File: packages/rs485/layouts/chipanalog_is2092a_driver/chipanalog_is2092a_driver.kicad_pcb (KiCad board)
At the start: 2 copper layers, 7 parts

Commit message: Rebuild all
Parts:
- turned U1 to 0 degrees
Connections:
- net hv-1 renamed VDDP
- net line renamed A
- net line-1 renamed DI
- net line-3 renamed RO
- net line-4 renamed B
- net transceiver-line renamed SEL
- C1 pad 1: hv -> VDDL
- C2 pad 1: hv-2 -> hv
- C4 pad 1: hv-2 -> hv
- C6 pad 1: hv-2 -> hv
- U1 pad 10: hv-2 -> hv
- U1 pad 11: hv-2 -> hv
- U1 pad 2: line-2 -> REh
- U1 pad 3: line-2 -> DE
- U1 pad 7: hv -> VDDL
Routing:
- net (no net): track 0.00 -> 13.7 mm
- net hv-2: track 5.88 -> 0.00 mm
- net VDDP: track 3.56 -> 0.00 mm
- net line-2: track 2.62 -> 0.00 mm
- net hv: track 1.65 -> 0.00 mm

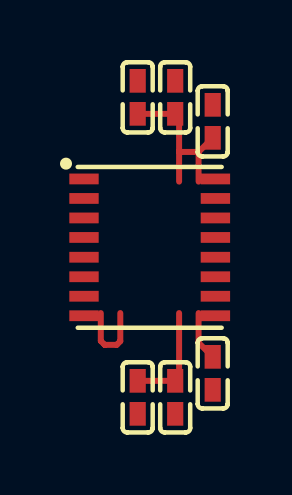
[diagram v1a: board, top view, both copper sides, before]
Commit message: Fix LDO power in voltage range
Fix RS485 sp3485 and is2092 RE WE connections
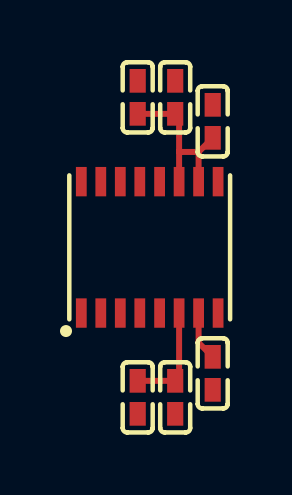
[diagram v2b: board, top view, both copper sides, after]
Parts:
- turned U1 to 90 degrees
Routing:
- net (no net): track 13.7 -> 0.00 mm
- net hv: track 0.00 -> 5.88 mm
- net VDDP: track 0.00 -> 3.56 mm
- net VDDL: track 0.00 -> 1.65 mm

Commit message: WIP update rs485
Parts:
- C1, C2: footprint atopile:C0402-b3ef17 -> Samsung_Electro_Mechanics_CL05A105KA5NQNC:C0402
- C3, C4: value 10µF ±20% 6.3V X5R -> 10µF ±20% 10V X5R; footprint atopile:C0402-b3ef17 -> Samsung_Electro_Mechanics_CL05A106MP5NUNC:C0402
- C5, C6: footprint atopile:C0402-b3ef17 -> Samsung_Electro_Mechanics_CL05B104KO5NNNC:C0402
- U1: footprint atopile:LGA-16_L5.2-W4.7-P0.65-TL_CA-IS2062A-FRANK2-ce0896 -> Chipanalog_CA_IS2092A:LGA-16_L5.2-W4.7-P0.65-TL_CA-IS2062A-FRANK2
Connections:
- C1 pad 2: gnd-1 -> gnd
- C2 pad 2: gnd -> gnd-1
- C3 pad 2: gnd-1 -> gnd
- C4 pad 2: gnd -> gnd-1
- C5 pad 2: gnd-1 -> gnd
- C6 pad 2: gnd -> gnd-1
- U1 pad 12: gnd -> gnd-1
- U1 pad 5: gnd-1 -> gnd
- U1 pad 8: gnd-1 -> gnd
- U1 pad 9: gnd -> gnd-1

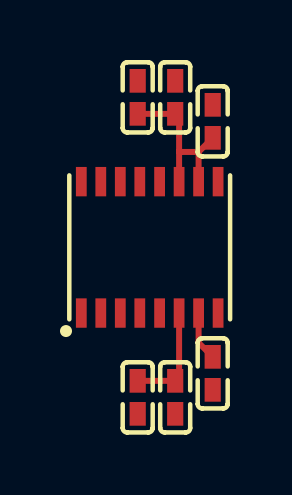
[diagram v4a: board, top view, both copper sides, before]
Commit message: Update 3D model locations
fix missing renders
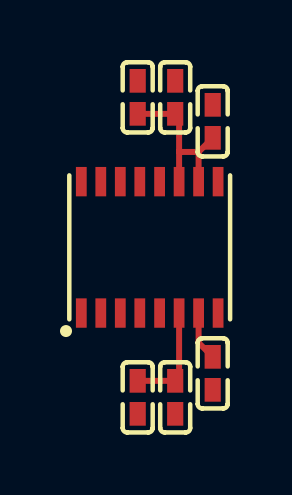
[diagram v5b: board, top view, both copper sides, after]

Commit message: rebuild all packages & regenerate images of changed layouts (silk)
Add new scripts for version bump and build (based on atopile/packages)
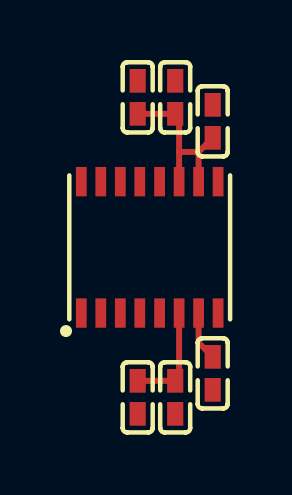
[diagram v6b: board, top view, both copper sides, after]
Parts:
- C3, C4: value 10µF ±20% 10V X5R -> 10µF ±20% 6.3V X5R; footprint Samsung_Electro_Mechanics_CL05A106MP5NUNC:C0402 -> Murata_Electronics_GRM155R60J106ME44D:C0402

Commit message: fix rs485 frozen build
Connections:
- net REh renamed nRE
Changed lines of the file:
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@@
     (net 1 "VDDL")
     (net 2 "DE")
-    (net 3 "REh")
+    (net 3 "nRE")
     (net 4 "gnd-1")
     (net 5 "gnd")
@@
             (size 0.98 0.36)
             (layers "F.Cu" "F.Paste" "F.Mask")
-            (net 3 "REh")
+            (net 3 "nRE")
         )
         (pad "3" smd rect
